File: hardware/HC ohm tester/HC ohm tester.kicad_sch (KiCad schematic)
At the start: 35 parts, among them J1 Conn_01x02_Pin, J2 Conn_01x02_Pin, J3 Conn_01x02_Pin, J4 DCPS+, J5 Conn_01x08_Pin, Q1 NTMFS0D8N03C, Q2 NTMFS0D8N03C, Q3 NTMFS0D8N03C, Q4 2N7002K, Q5 NTMFS0D8N03C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

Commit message: big relay alternative
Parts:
- removed Q1, Q2, Q5: NTMFS0D8N03C, Package_SO:ONSemi_SO-8FL_488AA, symbol HC_ohm_tester:NTMFS0D8N03CT1G
- removed Q4: 2N7002K, Package_TO_SOT_SMD:SOT-23, symbol Transistor_FET:2N7002K
- added Q1: 2N3904, Package_TO_SOT_SMD:SOT-363_SC-70-6, symbol Transistor_BJT:2N3904
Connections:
- net HC out is gone; now on net GND: J6.1 (Pin_1), Q3.1 (S), Q3.2 (S), Q3.3 (S)
- net +5V: now also Q1.3 (C)
- net HS active: now also Q1.2 (B)
- net at Q3.4 (G), R1.1: now also Q1.1 (E)
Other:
- note added: "batt+ 0v-14v"
- note removed: "DC PWR ---> switch ---> inductor ---> shunt ---> DUT ---> GND"
- note removed: "batt+ 0v-24v"
- note removed: "to inductor"
- moved on the sheet: C5, J2, J3, J4, J6, JP1, JP2, JP3, JP4, R1, R6, U1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

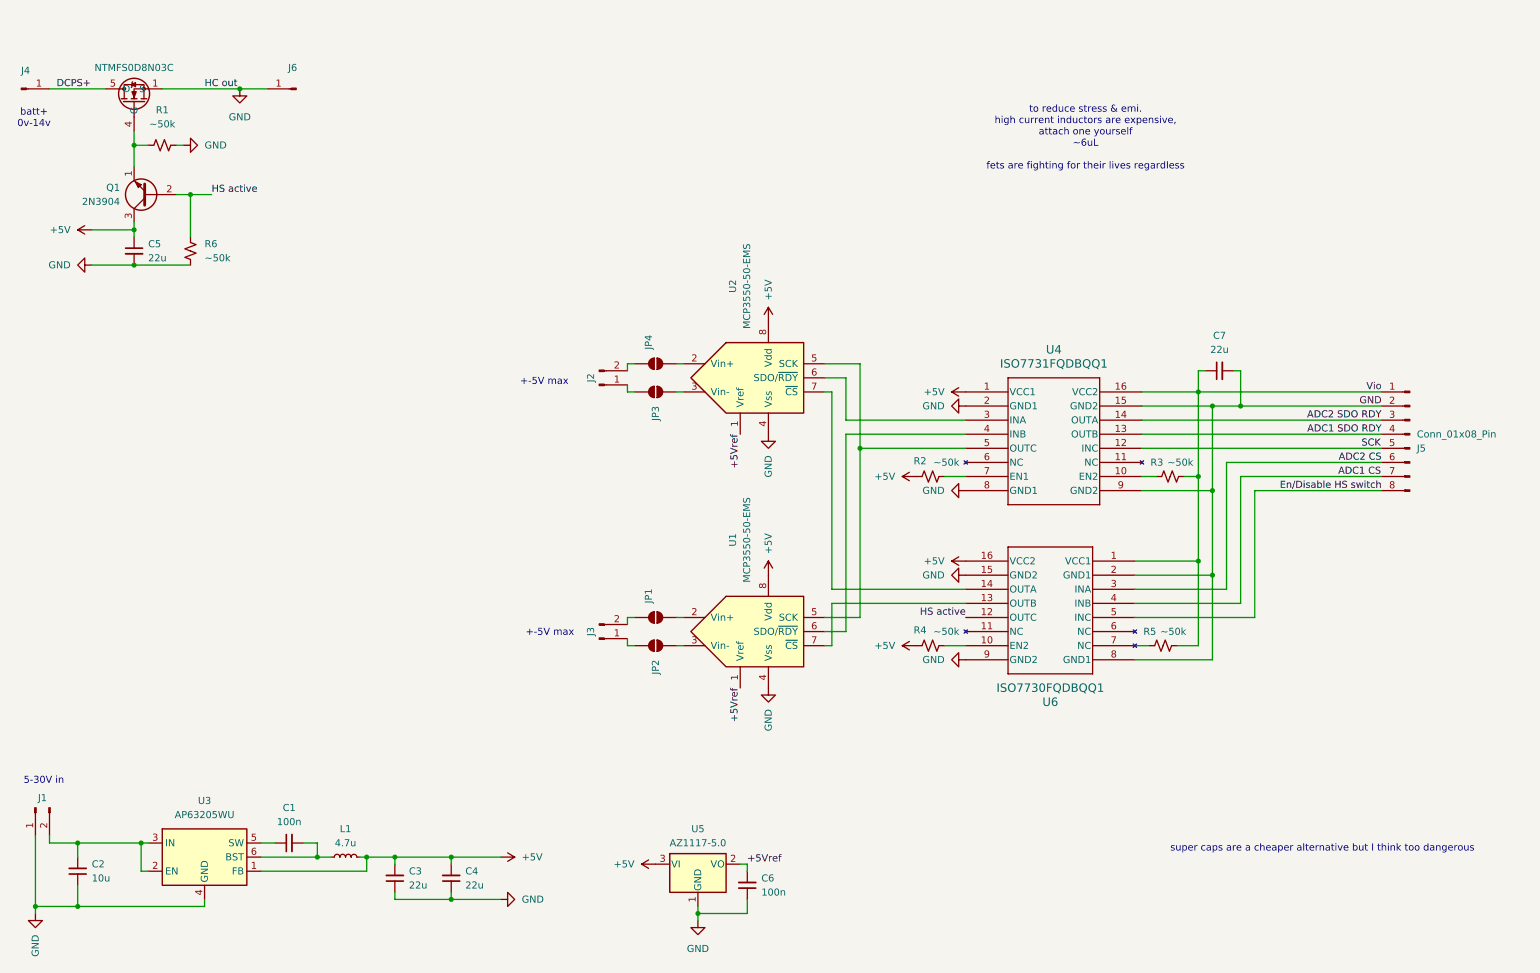
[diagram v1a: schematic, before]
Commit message: final revision A
board shipped using GDL, "across the globe eventually" at the small price of $5
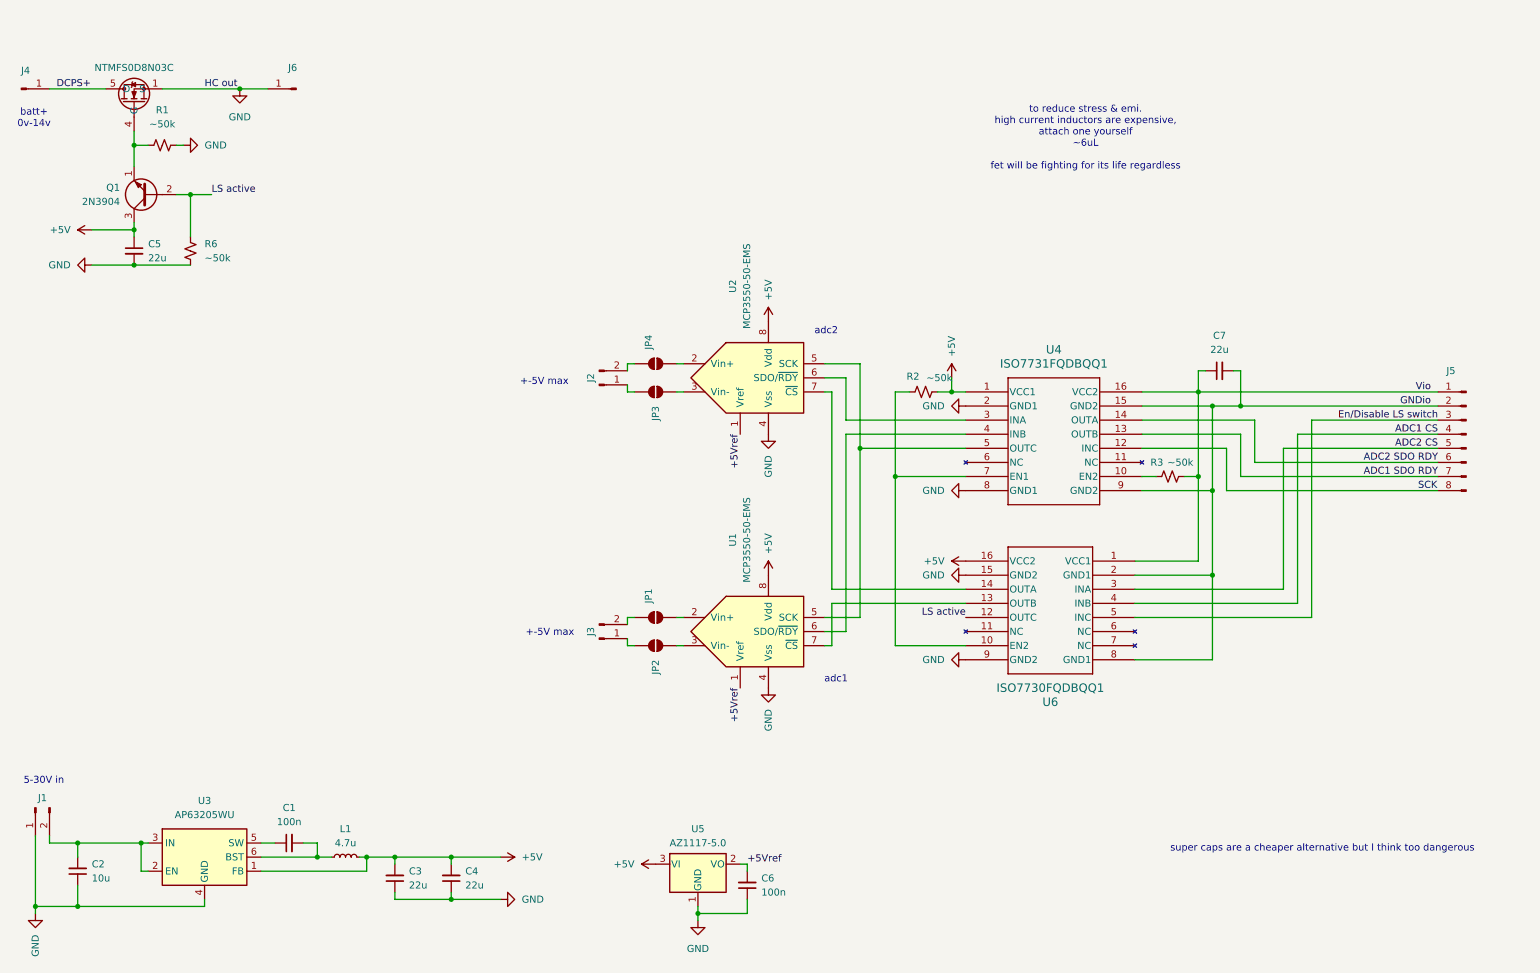
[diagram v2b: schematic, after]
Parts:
- removed R4, R5: ~50k, Resistor_SMD:R_1206_3216Metric_Pad1.30x1.75mm_HandSolder, symbol Device:R_Small_US
- L1: footprint Inductor_SMD:L_0201_0603Metric_Pad0.64x0.40mm_HandSolder -> Inductor_SMD:L_0603_1608Metric_Pad1.05x0.95mm_HandSolder
- Q1: footprint Package_TO_SOT_SMD:SOT-363_SC-70-6 -> Package_TO_SOT_THT:TO-92_Inline
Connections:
- net +5V: now also R2.1; no longer R2.2
- net ADC1 CS: now also J5.4 (Pin_4); no longer J5.7 (Pin_7)
- net ADC1 SDO RDY: now also J5.7 (Pin_7); no longer J5.4 (Pin_4)
- net ADC2 CS: now also J5.5 (Pin_5); no longer J5.6 (Pin_6)
- net ADC2 SDO RDY: now also J5.6 (Pin_6); no longer J5.3 (Pin_3)
- net GND: no longer C7.2, J5.2 (Pin_2), U4.15 (GND2), U4.9 (GND2), U6.2 (GND1), U6.8 (GND1)
- net SCK: now also J5.8 (Pin_8); no longer J5.5 (Pin_5)
- net at U4.7 (EN1): now also R2.2, U6.10 (EN2); no longer R2.1
- net En/Disable HS switch renamed En/Disable LS switch
- net En/Disable LS switch: now also J5.3 (Pin_3); no longer J5.8 (Pin_8)
- net HS active renamed LS active
- new net GNDio: C7.2, J5.2 (Pin_2), U4.15 (GND2), U4.9 (GND2), U6.2 (GND1), U6.8 (GND1)
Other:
- note added: "adc1"
- note added: "adc2"
- note added: "to reduce stress & emi. high current inductors are expensive, attach one yourself ~6uL fet will be fighting for its life regardless"
- note removed: "to reduce stress & emi. high current inductors are expensive, attach one yourself ~6uL fets are fighting for their lives regardless"
- moved on the sheet: J5, R2
